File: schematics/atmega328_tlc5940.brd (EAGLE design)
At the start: 125.7 x 63.2 mm, 40 parts, among them IC2 74LS595N, IC3 74HC165N, IC4 74HC165N, U1 ATMEGA328P_PDIP, U2 TLC5940-NT, U3 TLC5940-NT, U4 TLC5940-NT

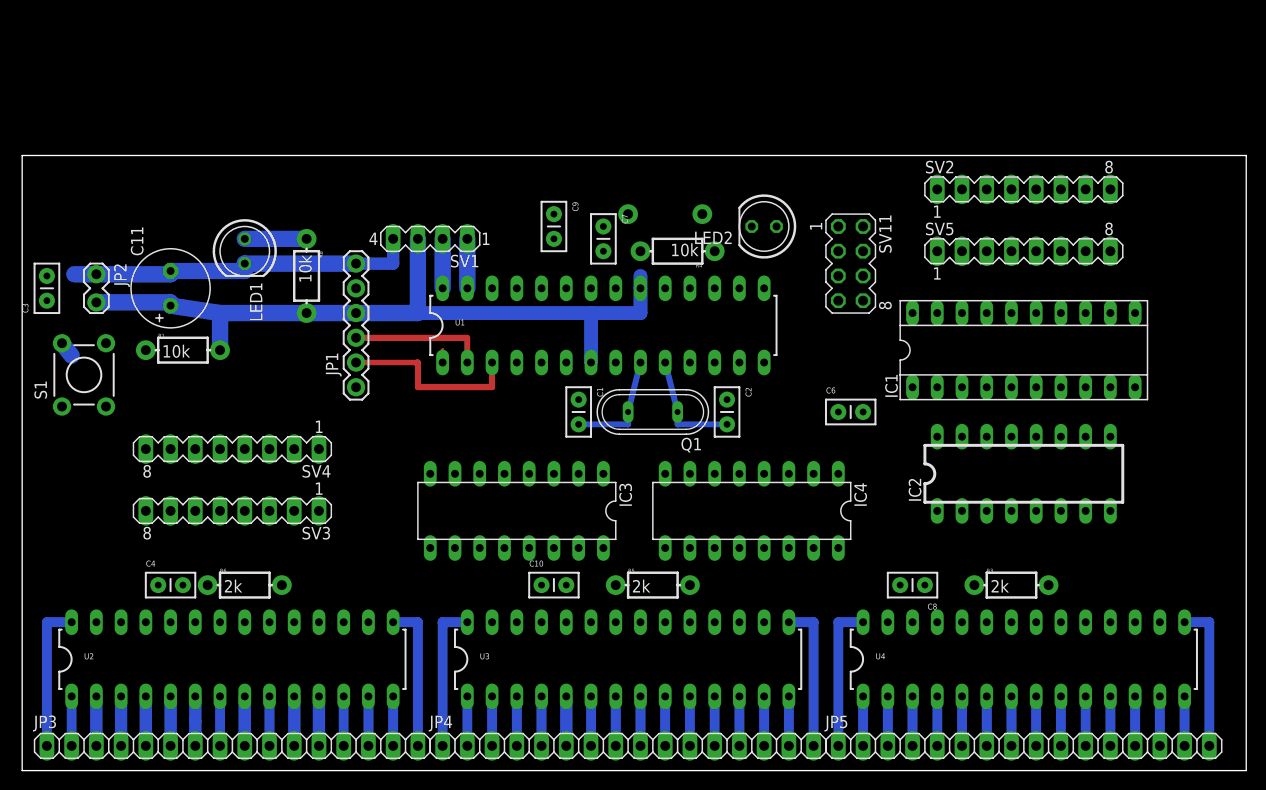
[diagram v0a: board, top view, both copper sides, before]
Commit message: update schematic with row scanning mechanism and tlc5940 pinout changes.   clock is shared with all SR's
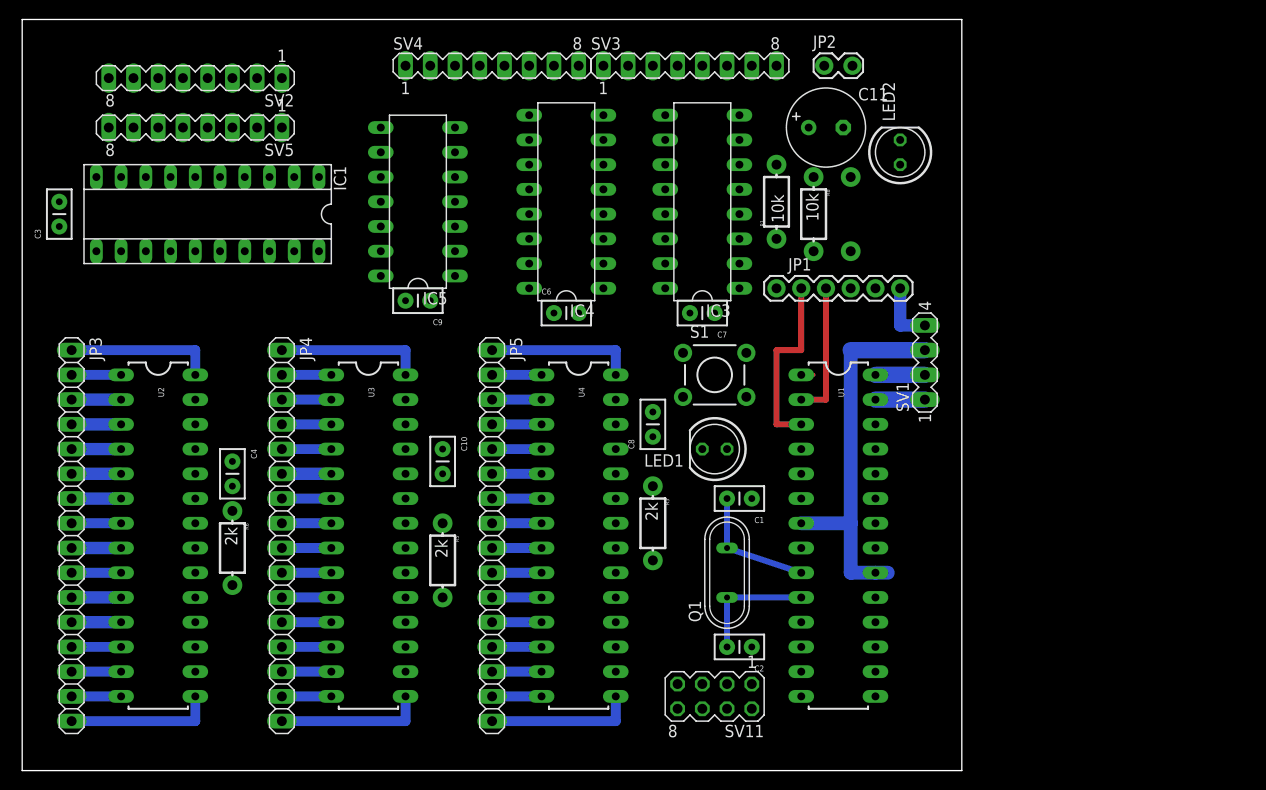
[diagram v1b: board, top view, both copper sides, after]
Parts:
- removed IC2: 74LS595N, SparkFun-DigitalIC:DIL16
- removed R4: 10k, SparkFun-Passives:AXIAL-0.3-KIT
- added IC5: 74HC164N, 74xx-us:DIL14
- moved SV5 86.0 mm to (17.8, 66.0), turned to 180 degrees
- moved SV2 85.9 mm to (17.8, 71.1), turned to 180 degrees
- moved IC1 85.0 mm to (19.1, 57.1), turned to 180 degrees
- moved JP2 78.0 mm to (82.5, 72.4), turned to 0 degrees
- moved C11 69.3 mm to (82.5, 66.0), turned to 0 degrees
- moved SV3 65.6 mm to (68.6, 72.4), turned to 0 degrees
- moved S1 64.8 mm to (71.1, 40.6), turned to 0 degrees
- moved R1 62.8 mm to (77.5, 58.4), turned to 90 degrees
- moved JP5 58.7 mm to (48.3, 24.1), turned to 270 degrees
- moved R8 52.5 mm to (81.3, 57.1)
- moved LED1 52.4 mm to (71.1, 33.0), turned to 180 degrees
- moved SV1 52.4 mm to (92.7, 41.9), turned to 90 degrees
- moved SV4 47.6 mm to (48.3, 72.4), turned to 0 degrees
- moved U4 47.5 mm to (57.1, 24.1), turned to 270 degrees
- moved SV11 46.6 mm to (71.1, 7.62), turned to 180 degrees
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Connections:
- removed net N$105: U1.17, U2.26
- removed net N$71: IC1.10, U1.26
- removed net N$96: IC3.10, U1.18
- removed net N$98: IC4.10
- removed net N$99: IC3.1, IC4.1, U1.4
- removed net TX$0: JP1.RXI, U1.3
- new net N$61: IC4.1, U1.17
- new net N$70: IC3.10, U1.16
- new net SIN: JP1.RXI, U1.3, U2.26
- net BLANK: now also U1.12; no longer R4.P$1, U1.16
- net DCPRG: now also U1.5
- net GND: now also IC4.15, IC5.7; no longer IC2.13, IC2.8
- net GSCLK: now also U1.14; no longer U1.5
- net N$58: now also IC5.3; no longer IC2.15
- net N$59: now also IC5.2, U1.18; no longer IC3.9
- net N$60: now also IC1.10, IC4.2, IC5.8, U1.19; no longer IC2.12, U1.24
- net N$62: now also IC5.4; no longer IC2.1
- net N$63: now also IC5.5; no longer IC2.2
- net N$64: now also IC5.6; no longer IC2.3
- net N$65: now also IC5.10; no longer IC2.4
- net N$66: now also IC5.11; no longer IC2.5
- net N$67: now also IC5.12; no longer IC2.6
- net N$68: now also IC5.13; no longer IC2.7
- net N$69: now also IC3.9, IC4.10; no longer IC2.14, U1.23
- net SCLK: now also U1.11; no longer IC2.11, IC3.2, IC4.2, U1.19
- net VCC: now also IC5.1, IC5.14; no longer IC2.10, IC2.16, R4.P$2
- net VPRG: now also U1.13
- net XLAT: now also U1.6; no longer U1.15
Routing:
- net VCC: track 76.6 -> 39.4 mm
- net GND: track 38.0 -> 6.35 mm
- net SIN: track 0.00 -> 19.1 mm
- net TX$0: track 19.0 -> 0.00 mm
- net N$56: track 6.35 -> 0.00 mm
- net N$2: track 11.6 -> 13.1 mm
- net N$3: track 11.6 -> 12.7 mm
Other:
- board size 125.7 x 63.2 mm -> 96.5 x 77.1 mm
